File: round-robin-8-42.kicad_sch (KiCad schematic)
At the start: 98 parts

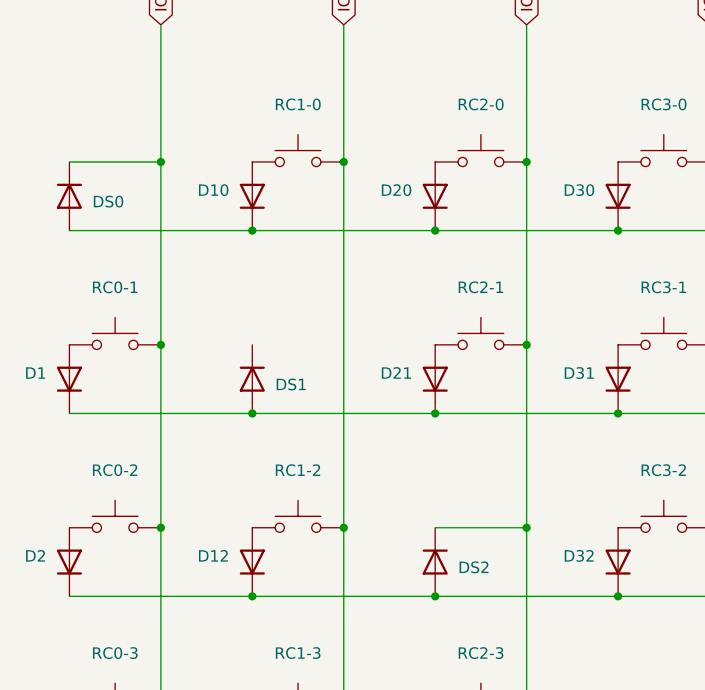
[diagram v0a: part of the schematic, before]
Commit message: Add missing connector on DS1
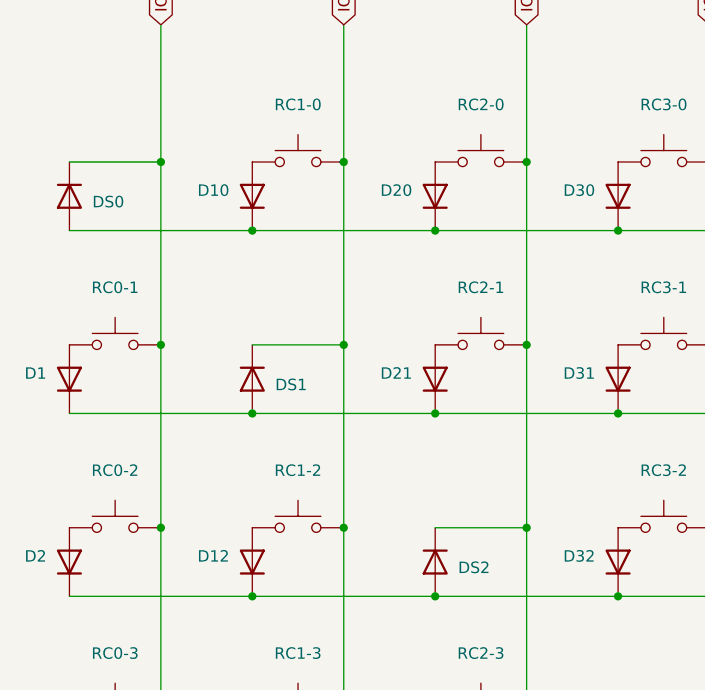
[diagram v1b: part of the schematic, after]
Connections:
- net IO 1: now also DS1.1 (K)
